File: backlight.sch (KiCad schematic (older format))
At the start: 12 parts, among them P1 CONN_01X05, U1 APA102C, U2 APA102C, U3 APA102C, U4 APA102C, U5 APA102C, U6 APA102C, U7 APA102C, U8 APA102C, U9 APA102C

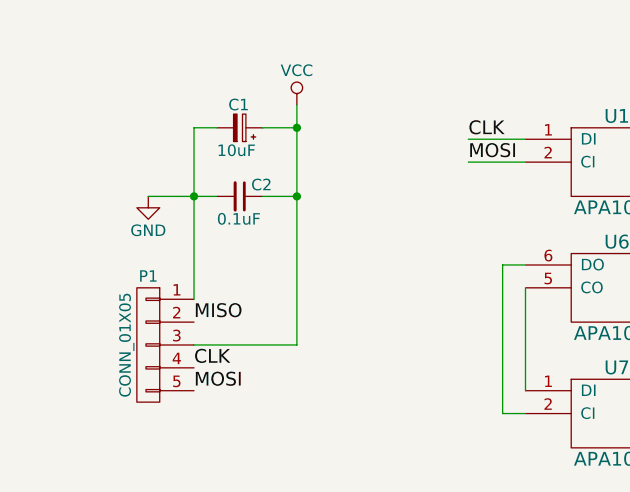
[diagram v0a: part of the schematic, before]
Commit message: Modified pcb design for easy solidering
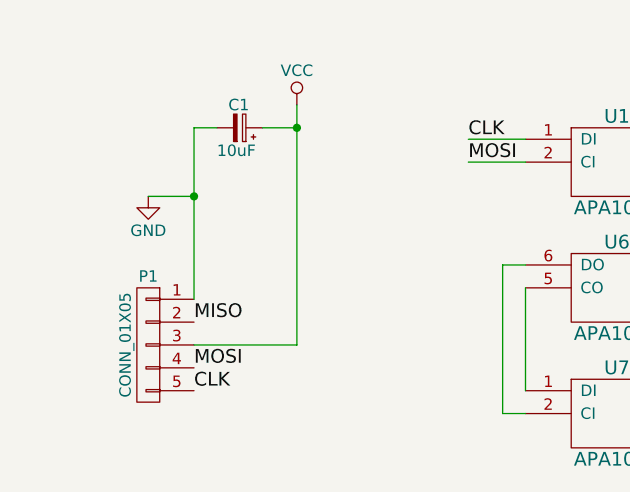
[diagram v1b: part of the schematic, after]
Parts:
- removed C2: 0.1uF, Capacitors_SMD:C_0402, symbol C_Small
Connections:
- net CLK: now also P1.5 (P5); no longer P1.4 (P4)
- net MOSI: now also P1.4 (P4); no longer P1.5 (P5)
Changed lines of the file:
@@
 $EndComp
-$Comp
-L C_Small C2
-U 1 1 57569AF5
-P 2150 3000
-F 0 "C2" V 2100 3050 50  0000 L CNN
-F 1 "0.1uF" V 2250 2900 50  0000 L CNN
-F 2 "Capacitors_SMD:C_0402" H 2150 3000 50  0001 C CNN
-F 3 "" H 2150 3000 50  0000 C CNN
-	1    2150 3000
-	0    1    1    0
-$EndComp
-Wire Wire Line
-	1950 2700 2050 2700
 $Comp
 L GND #PWR04
@@
 	1    0    0    -1
 $EndComp
-Wire Wire Line
-	2250 2700 2400 2700
-Wire Wire Line
-	1750 3000 2050 3000
-Connection ~ 1950 3000
-Wire Wire Line
-	2250 3000 2400 3000
-Connection ~ 2400 3000
-Wire Wire Line
-	6200 2850 6200 3300
-Wire Wire Line
-	6200 2750 6300 2750
-Wire Wire Line
-	6300 2750 6300 3400
-Wire Wire Line
-	6300 3400 6200 3400
-Wire Wire Line
-	3400 3400 3400 3850
-Wire Wire Line
-	3400 3300 3300 3300
-Wire Wire Line
-	3300 3300 3300 3950
-Wire Wire Line
-	3300 3950 3400 3950
 NoConn ~ 6200 3950
 $Comp
@@
 Text Label 6200 3850 0    60   ~ 0
 MISO
-Wire Wire Line
-	1950 1000 1950 1150
 $Comp
 L PWR_FLAG #FLG05
@@
 	1    0    0    -1
 $EndComp
+Text Label 1950 3750 0    60   ~ 0
+MOSI
+Text Label 1950 3850 0    60   ~ 0
+CLK
+Text Label 3150 2750 0    60   ~ 0
+CLK
+Text Label 3150 2850 0    60   ~ 0
+MOSI
+Wire Wire Line
+	1950 2700 2050 2700
+Wire Wire Line
+	2250 2700 2400 2700
+Wire Wire Line
+	6200 2850 6200 3300
+Wire Wire Line
+	6200 2750 6300 2750
+Wire Wire Line
+	6300 2750 6300 3400
+Wire Wire Line
+	6300 3400 6200 3400
+Wire Wire Line
+	3400 3400 3400 3850
+Wire Wire Line
+	3400 3300 3300 3300
+Wire Wire Line
+	3300 3300 3300 3950
+Wire Wire Line
+	3300 3950 3400 3950
+Wire Wire Line
+	1950 1000 1950 1150
 Wire Wire Line
 	1400 1000 1400 1150
@@
 Wire Wire Line
 	5200 3950 5400 3950
-Text Label 1950 3850 0    60   ~ 0
-MOSI
-Text Label 1950 3750 0    60   ~ 0
-CLK
-Text Label 3150 2750 0    60   ~ 0
-CLK
 Wire Wire Line
 	3150 2750 3400 2750
-Text Label 3150 2850 0    60   ~ 0
-MOSI
 Wire Wire Line
 	3150 2850 3400 2850
@@
 Wire Wire Line
 	2400 3650 1950 3650
+Wire Wire Line
+	1750 3000 1950 3000
+Connection ~ 1950 3000
 $EndSCHEMATC

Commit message: Fixed connection error
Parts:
- P1: footprint Connectors_Molex:Molex_Panelmate-53780-0570_05x1.25mm_Angled -> Connectors_Molex:Molex_Panelmate-53780-0470_04x1.25mm_Angled; symbol CONN_01X05 -> CONN_01X04
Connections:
- net CLK: now also P1.3 (P3), U1.2 (CI); no longer P1.5 (P5), U1.1 (DI)
- net MOSI: now also U1.1 (DI); no longer U1.2 (CI)
- net VCC: now also P1.2 (P2); no longer P1.3 (P3)
- net at U3.5 (CO): now also U4.2 (CI); no longer U4.1 (DI)
- net at U3.6 (DO): now also U4.1 (DI); no longer U4.2 (CI)
- net at U6.5 (CO): now also U7.2 (CI); no longer U7.1 (DI)
- net at U6.6 (DO): now also U7.1 (DI); no longer U7.2 (CI)
- net MISO: no longer names the net of U9.6 (DO)
- net MISO: no longer P1.2 (P2)
- no-connect marks 1 -> 2
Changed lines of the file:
@@
 LIBS:valves
 LIBS:superled
-LIBS:backlight-cache
 EELAYER 25 0
 EELAYER END
@@
 NoConn ~ 6200 3950
 $Comp
-L CONN_01X05 P1
+L CONN_01X04 P1
 U 1 1 5756AF90
-P 1750 3650
-F 0 "P1" H 1750 3950 50  0000 C CNN
-F 1 "CONN_01X05" V 1850 3650 50  0000 C CNN
-F 2 "Connectors_Molex:Molex_Panelmate-53780-0570_05x1.25mm_Angled" H 1750 3650 50  0001 C CNN
-F 3 "" H 1750 3650 50  0000 C CNN
-	1    1750 3650
-	-1   0    0    -1
-$EndComp
-Text Label 1950 3550 0    60   ~ 0
-MISO
-Text Label 6200 3850 0    60   ~ 0
-MISO
+P 1750 3700
+F 0 "P1" H 1750 4000 50  0000 C CNN
+F 1 "CONN_01X05" V 1850 3700 50  0000 C CNN
+F 2 "Connectors_Molex:Molex_Panelmate-53780-0470_04x1.25mm_Angled" H 1750 3700 50  0001 C CNN
+F 3 "" H 1750 3700 50  0000 C CNN
+	1    1750 3700
+	-1   0    0    -1
+$EndComp
 $Comp
 L PWR_FLAG #FLG05
@@
 $EndComp
 Text Label 1950 3750 0    60   ~ 0
+CLK
+Text Label 1950 3850 0    60   ~ 0
 MOSI
-Text Label 1950 3850 0    60   ~ 0
+Text Label 3150 2750 0    60   ~ 0
+MOSI
+Text Label 3150 2850 0    60   ~ 0
 CLK
-Text Label 3150 2750 0    60   ~ 0
-CLK
-Text Label 3150 2850 0    60   ~ 0
-MOSI
 Wire Wire Line
 	1950 2700 2050 2700
@@
 	2250 2700 2400 2700
 Wire Wire Line
-	6200 2850 6200 3300
-Wire Wire Line
 	6200 2750 6300 2750
 Wire Wire Line
-	6300 2750 6300 3400
-Wire Wire Line
-	6300 3400 6200 3400
-Wire Wire Line
-	3400 3400 3400 3850
-Wire Wire Line
 	3400 3300 3300 3300
-Wire Wire Line
-	3300 3300 3300 3950
-Wire Wire Line
-	3300 3950 3400 3950
 Wire Wire Line
 	1950 1000 1950 1150
@@
 Connection ~ 2400 2700
 Wire Wire Line
-	1950 2700 1950 3450
+	1950 2700 1950 3550
 Wire Wire Line
 	2400 2600 2400 3650
@@
 	1750 3000 1950 3000
 Connection ~ 1950 3000
+Wire Wire Line
+	6300 2750 6300 3300
+Wire Wire Line
+	6300 3300 6200 3300
+Wire Wire Line
+	6200 2850 6400 2850
+Wire Wire Line
+	6400 2850 6400 3400
+Wire Wire Line
+	6400 3400 6200 3400
+Wire Wire Line
+	3300 3300 3300 3850
+Wire Wire Line
+	3300 3850 3400 3850
+Wire Wire Line
+	3400 3400 3200 3400
+Wire Wire Line
+	3200 3400 3200 3950
+Wire Wire Line
+	3200 3950 3400 3950
+NoConn ~ 6200 3850
 $EndSCHEMATC
